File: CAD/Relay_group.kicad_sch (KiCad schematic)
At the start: 2 parts, among them U1 TPIC6C596

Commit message: new relays
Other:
- company: (none) -> NMBU-Mina
- title: (none) -> SPI-MUX
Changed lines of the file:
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@@
 (kicad_sch (version 20211123) (generator eeschema)
   (paper "A4")
+  (title_block
+    (title "SPI-MUX")
+    (date "2023-02-06")
+    (rev "0.01")
+    (company "NMBU-Mina")
+    (comment 1 "F.N.Beilegaard")
+  )
   (wire (pts (xy 113.03 102.87) (xy 119.38 102.87))
     (stroke (width 0) (type default) (color 0 0 0 0))

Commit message: Feat:Fixed digikey partnumbers, rexport, 3d mod
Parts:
- C1: Digikey (none) -> CL10B104KB8NFNC; LCSC Part # (none) -> CL10B104KB8NFNC
- U1: Digikey (none) -> TPIC6C596PWR; LCSC Part # (none) -> TPIC6C596PWR
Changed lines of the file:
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@@
+      (effects (font (size 1.27 1.27)) hide)
+    )
+    (property "Digikey" "TPIC6C596PWR" (id 4) (at 100.33 96.52 0)
+      (effects (font (size 1.27 1.27)) hide)
+    )
+    (property "LCSC Part #" "TPIC6C596PWR" (id 5) (at 100.33 96.52 0)
       (effects (font (size 1.27 1.27)) hide)
     )
@@
       (effects (font (size 1.27 1.27)) hide)
     )
+    (property "Digikey" "CL10B104KB8NFNC" (id 4) (at 72.39 123.19 0)
+      (effects (font (size 1.27 1.27)) hide)
+    )
+    (property "LCSC Part #" "CL10B104KB8NFNC" (id 5) (at 72.39 123.19 0)
+      (effects (font (size 1.27 1.27)) hide)
+    )

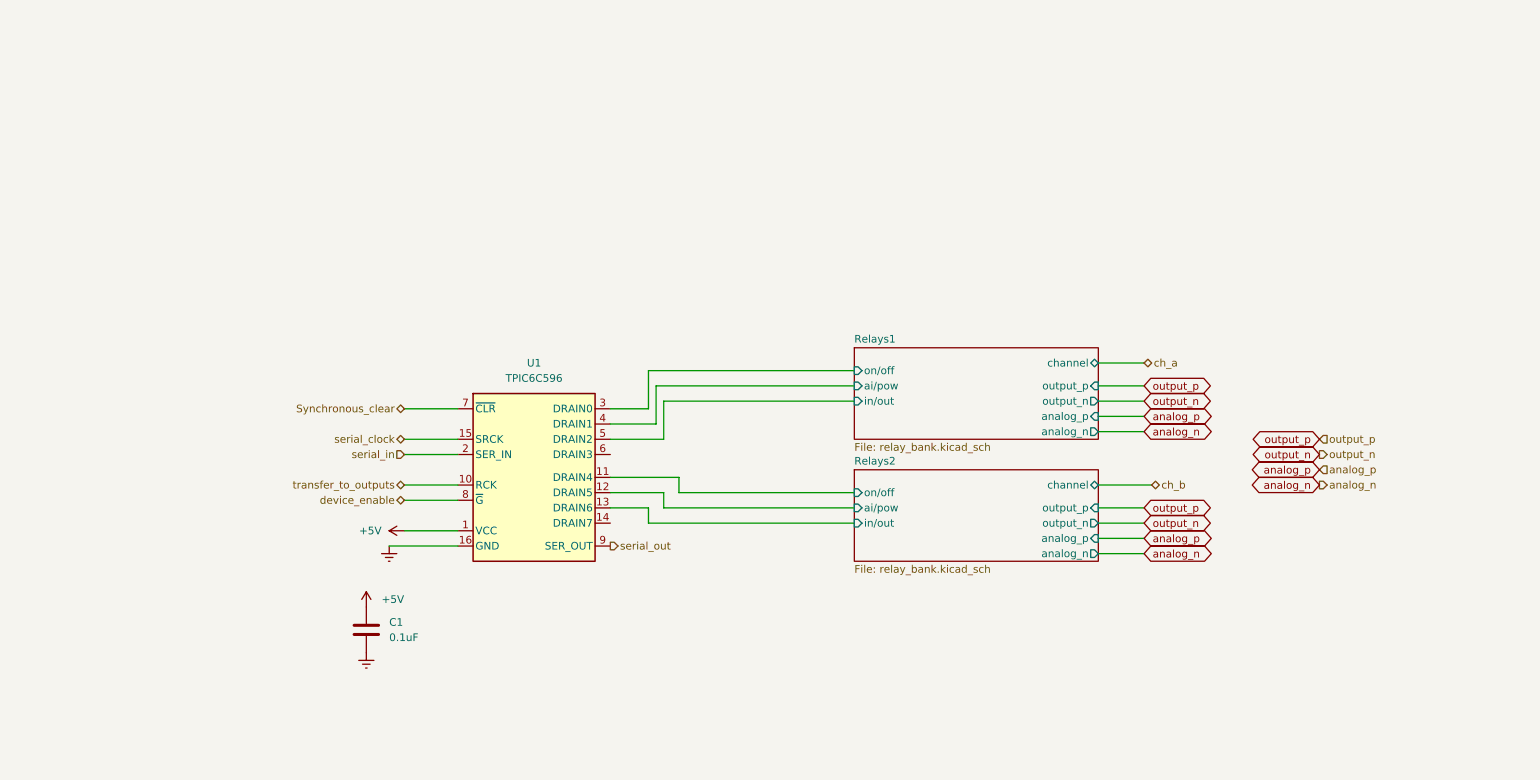
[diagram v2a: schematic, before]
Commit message: Feat: Single side test
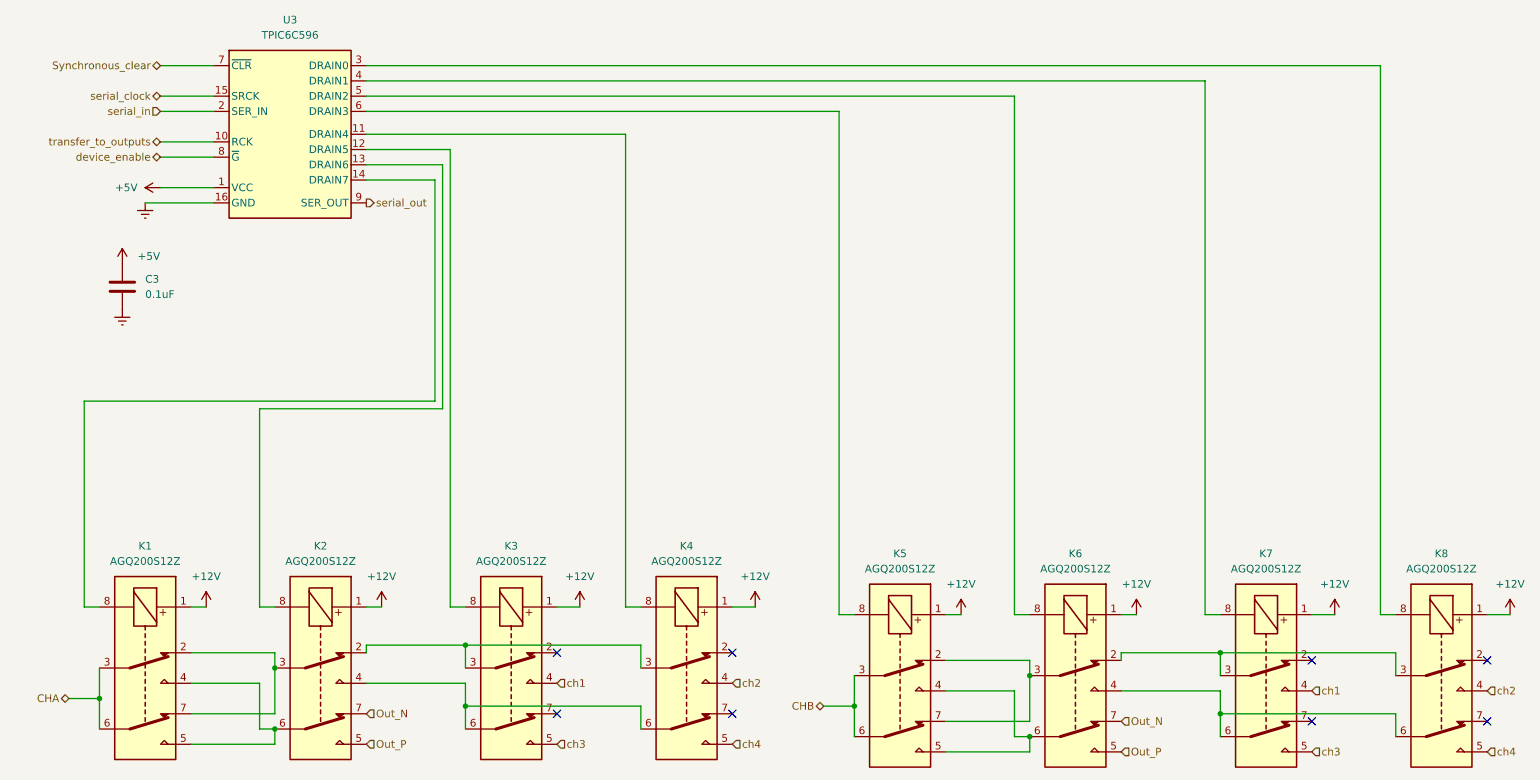
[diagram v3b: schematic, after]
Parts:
- added K1, K2, K3, K4, K5, K6, K7, K8: AGQ200S12Z, muxlib_footprints:Relay_2P2T_10x6mm_TE_IMxxG, symbol muxlib:AGQ200S12Z
- renumbered C1 to C3, U1 to U3
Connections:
- net at U3.14 (DRAIN7): now also K1.8
- net at U3.6 (DRAIN3): now also K5.8
- net Relays1/ai/pow: no longer names the net of U3.4 (DRAIN1)
- net Relays1/ai/pow: now also K7.8
- net Relays1/in/out: no longer names the net of U3.5 (DRAIN2)
- net Relays1/in/out: now also K6.8
- net Relays1/on/off: no longer names the net of U3.3 (DRAIN0)
- net Relays1/on/off: now also K8.8
- net Relays2/ai/pow: no longer names the net of U3.12 (DRAIN5)
- net Relays2/ai/pow: now also K3.8
- net Relays2/in/out: no longer names the net of U3.13 (DRAIN6)
- net Relays2/in/out: now also K2.8
- net Relays2/on/off: no longer names the net of U3.11 (DRAIN4)
- net Relays2/on/off: now also K4.8
- new net: K6.2, K7.3, K8.3
- new net: K6.4, K7.6, K8.6
- new net: K5.2, K5.7, K6.3
- new net: K5.4, K5.5, K6.6
- new net: K2.2, K3.3, K4.3
- new net: K2.4, K3.6, K4.6
- new net: K1.2, K1.7, K2.3
- new net: K1.4, K1.5, K2.6
- new net +12V: K1.1, K2.1, K3.1, K4.1, K5.1, K6.1, K7.1, K8.1
- new net CHA: K1.3, K1.6
- new net CHB: K5.3, K5.6
- new net Out_N: K2.7, K6.7
- new net Out_P: K2.5, K6.5
- new net ch1: K3.4, K7.4
- new net ch2: K4.4, K8.4
- new net ch3: K3.5, K7.5
- new net ch4: K4.5, K8.5
- no-connect marks 0 -> 8
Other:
- removed sheet Relays1
- removed sheet Relays2
- moved on the sheet: C3, U3
